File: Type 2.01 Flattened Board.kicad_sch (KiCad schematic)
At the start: 4 parts

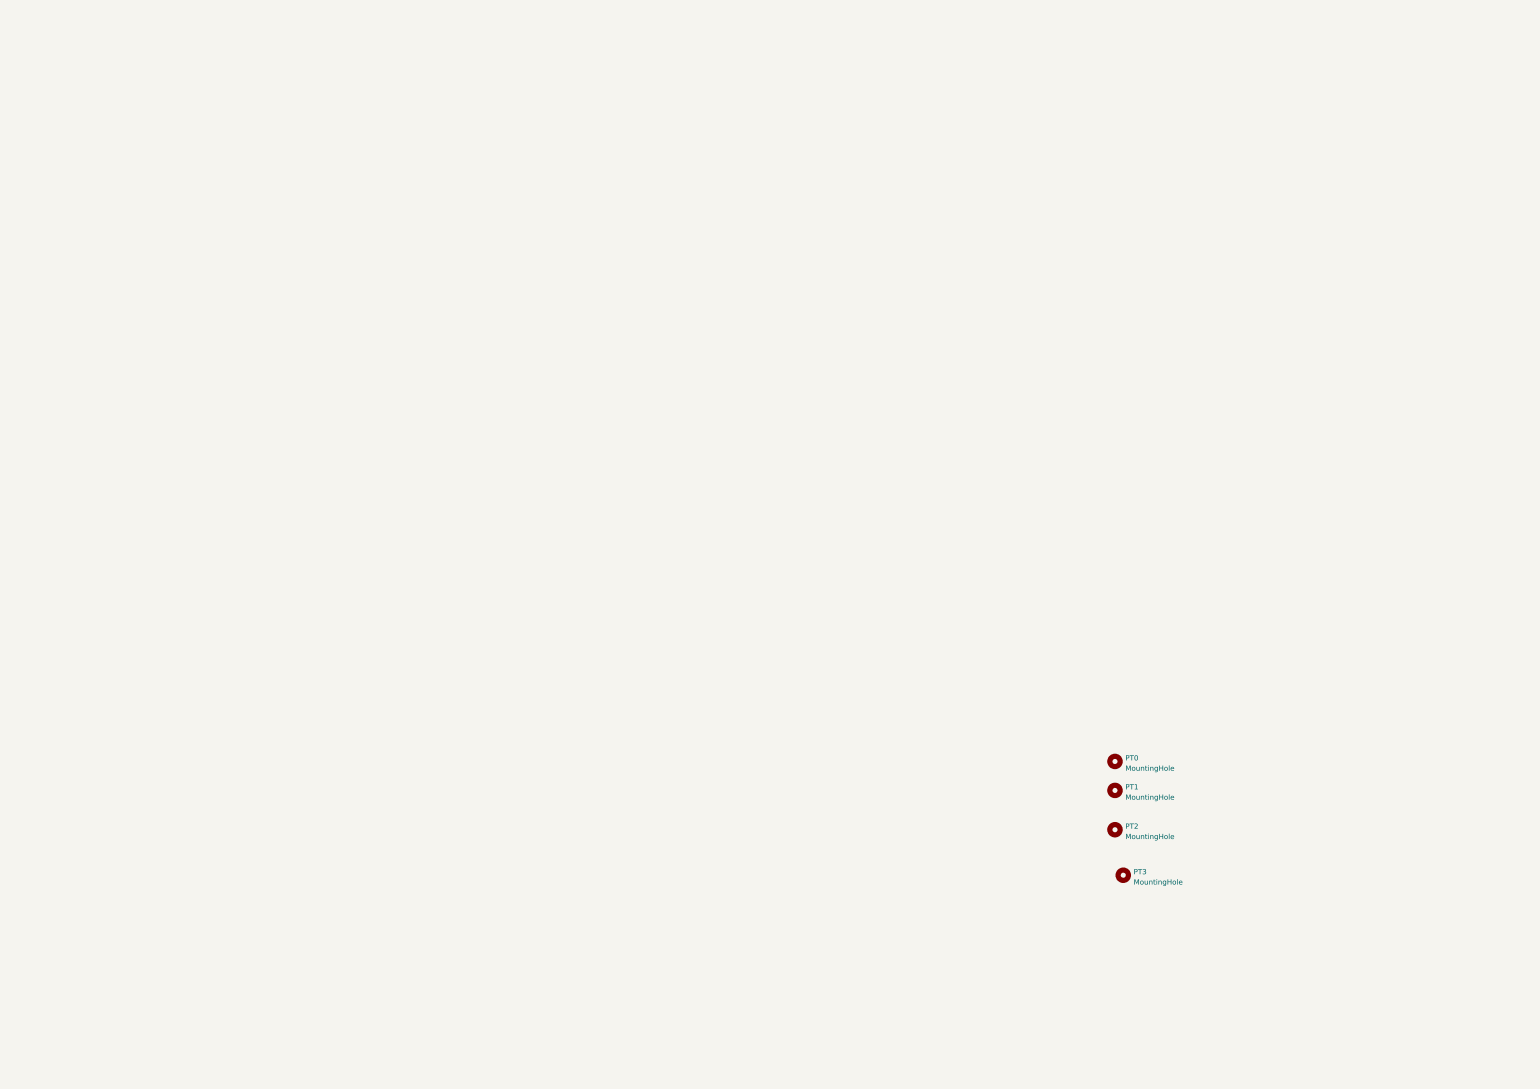
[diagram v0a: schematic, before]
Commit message: Start defining the pinout of the grand central m4
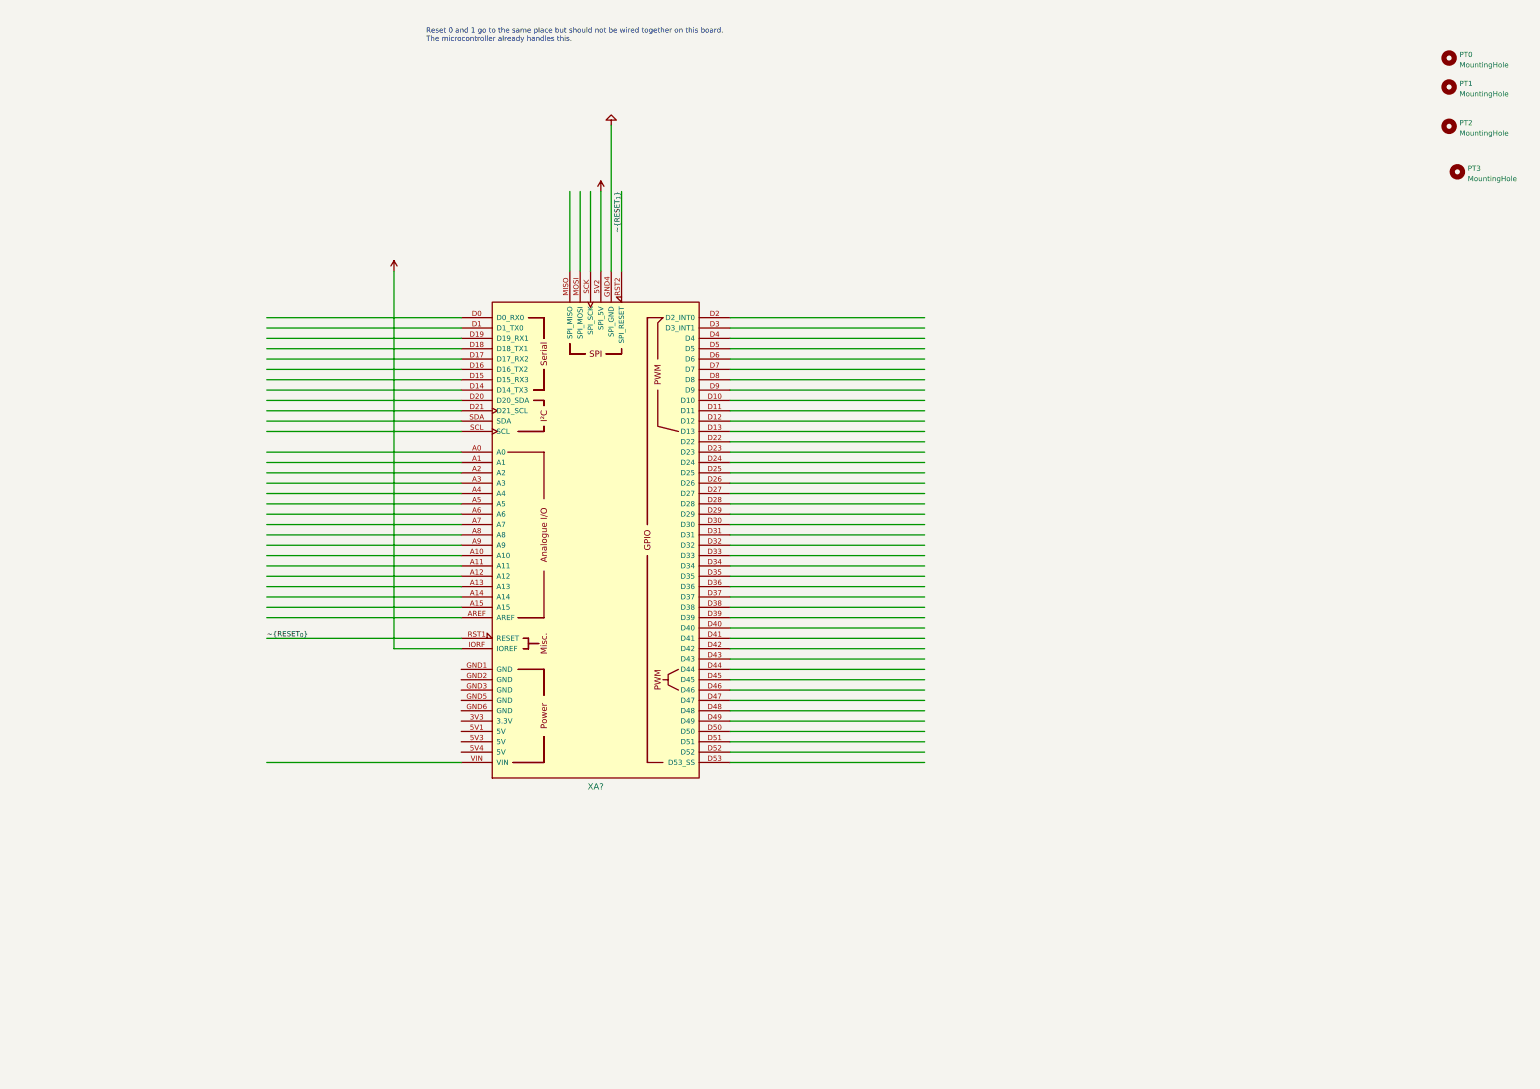
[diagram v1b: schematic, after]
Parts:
- added XA?: (no value), symbol arduino_alarm_siren:Arduino_Mega2560_Shield
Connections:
- new net +5V: XA?.5V2 (SPI_5V)
- new net GND: XA?.GND4 (SPI_GND)
- new net VCC: XA?.IORF (IOREF)
- new net ~{RESET_{0}}: XA?.RST1 (RESET)
- new net ~{RESET_{1}}: XA?.RST2 (SPI_RESET)
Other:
- note added: "Reset 0 and 1 go to the same place but should not be wired together on this board. The microcontroller already handles this."
- moved on the sheet: PT0, PT1, PT2, PT3

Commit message: More bus pin out action
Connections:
- net +5V: now also XA?.5V1 (5V), XA?.5V3 (5V), XA?.5V4 (5V)
- net GND: now also XA?.GND1 (GND), XA?.GND2 (GND), XA?.GND3 (GND), XA?.GND5 (GND), XA?.GND6 (GND)
- net +3V3: now reaches XA?.3V3 (3.3V)
- net Analog0: now reaches XA?.A0
- net Analog1: now reaches XA?.A1
- net Analog10: now reaches XA?.A10
- net Analog11: now reaches XA?.A11
- net Analog12: now reaches XA?.A12
- net Analog13: now reaches XA?.A13
- net Analog14: now reaches XA?.A14
- net Analog15: now reaches XA?.A15
- net Analog2: now reaches XA?.A2
- net Analog3: now reaches XA?.A3
- net Analog4: now reaches XA?.A4
- net Analog5: now reaches XA?.A5
- net Analog6: now reaches XA?.A6
- net Analog7: now reaches XA?.A7
- net Analog8: now reaches XA?.A8
- net Analog9: now reaches XA?.A9
- net AREF: now reaches XA?.AREF
- net BUS.PB25: now reaches XA?.D0 (D0_RX0)
- net BUS.PB24: now reaches XA?.D1 (D1_TX0)
- net BUS.PB22: now reaches XA?.D10
- net BUS.PB23: now reaches XA?.D11
- net D12: now reaches XA?.D12
- net D13: now reaches XA?.D13
- net D14: now reaches XA?.D14 (D14_TX3)
- net D15: now reaches XA?.D15 (D15_RX3)
- net D16: now reaches XA?.D16 (D16_TX2)
- net D17: now reaches XA?.D17 (D17_RX2)
- net D18: now reaches XA?.D18 (D18_TX1)
- net D19: now reaches XA?.D19 (D19_RX1)
- net BUS.PC18: now reaches XA?.D2 (D2_INT0)
- net BUS.PB20: now reaches XA?.D20 (D20_SDA)
- net BUS.PB21: now reaches XA?.D21 (D21_SCL)
- net BUS.PD12: now reaches XA?.D22
- net BUS.PA15: now reaches XA?.D23
- net BUS.PC17: now reaches XA?.D24
- net BUS.PC16: now reaches XA?.D25
- net D26: now reaches XA?.D26
- net D27: now reaches XA?.D27
- net D28: now reaches XA?.D28
- net D29: now reaches XA?.D29
- net BUS.PC19: now reaches XA?.D3 (D3_INT1)
- net D30: now reaches XA?.D30
- net D31: now reaches XA?.D31
- net D32: now reaches XA?.D32
- net D33: now reaches XA?.D33
- net D34: now reaches XA?.D34
- net D35: now reaches XA?.D35
- net D36: now reaches XA?.D36
- net D37: now reaches XA?.D37
- net D38: now reaches XA?.D38
- net D39: now reaches XA?.D39
- net BUS.PC20: now reaches XA?.D4
- net D40: now reaches XA?.D40
- net D41: now reaches XA?.D41
- net D42: now reaches XA?.D42
- net D43: now reaches XA?.D43
- net BUS.PC11: now reaches XA?.D44
- net BUS.PC10: now reaches XA?.D45
- net BUS.PC06: now reaches XA?.D46
- net BUS.PC07: now reaches XA?.D47
- net BUS.PC04: now reaches XA?.D48
- net BUS.PC05: now reaches XA?.D49
- net BUS.PC21: now reaches XA?.D5
- net MISO: now reaches XA?.D50
- net MOSI: now reaches XA?.D51
- net SCK: now reaches XA?.D52
- net ~{CS}: now reaches XA?.D53 (D53_SS)
- net BUS.PD20: now reaches XA?.D6
- net BUS.PD21: now reaches XA?.D7
- net BUS.PB18: now reaches XA?.D8
- net D9: now reaches XA?.D9
- net SPI_MISO: now reaches XA?.MISO (SPI_MISO)
- net SPI_MOSI: now reaches XA?.MOSI (SPI_MOSI)
- net SPI_SCK: now reaches XA?.SCK (SPI_SCK)
- net SCL_UNO: now reaches XA?.SCL
- net SDA_UNO: now reaches XA?.SDA
- net VIN: now reaches XA?.VIN
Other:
- note added: "Reset 0 and 1 go to the same place but should not be wired together on this board. The microcontroller already handles this. Same thing with SDA/SCL and the ICSP and miso connectors"
- note removed: "Reset 0 and 1 go to the same place but should not be wired together on this board. The microcontroller already handles this."

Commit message: Got the bus pinout done
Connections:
- net D12 renamed BUS.PB0
- net D13 renamed BUS.PB1
- net D14 renamed BUS.PB16
- net D15 renamed BUS.PB17
- net D16 renamed BUS.PC22
- net D17 renamed BUS.PC23
- net D18 renamed BUS.PB12
- net D19 renamed BUS.PB13
- net D26 renamed BUS.PA12
- net D27 renamed BUS.PA13
- net D28 renamed BUS.PA14
- net D29 renamed BUS.PB19
- net D30 renamed BUS.PA23
- net D31 renamed BUS.PA22
- net D32 renamed BUS.PA21
- net D33 renamed BUS.PA20
- net D34 renamed BUS.PA19
- net D35 renamed BUS.PA18
- net D36 renamed BUS.PA17
- net D37 renamed BUS.PA16
- net D38 renamed BUS.PB15
- net D39 renamed BUS.PB14
- net D40 renamed BUS.PC13
- net D41 renamed BUS.PC12
- net D42 renamed BUS.PC15
- net D43 renamed BUS.PC14
- net D9 renamed BUS.PB2

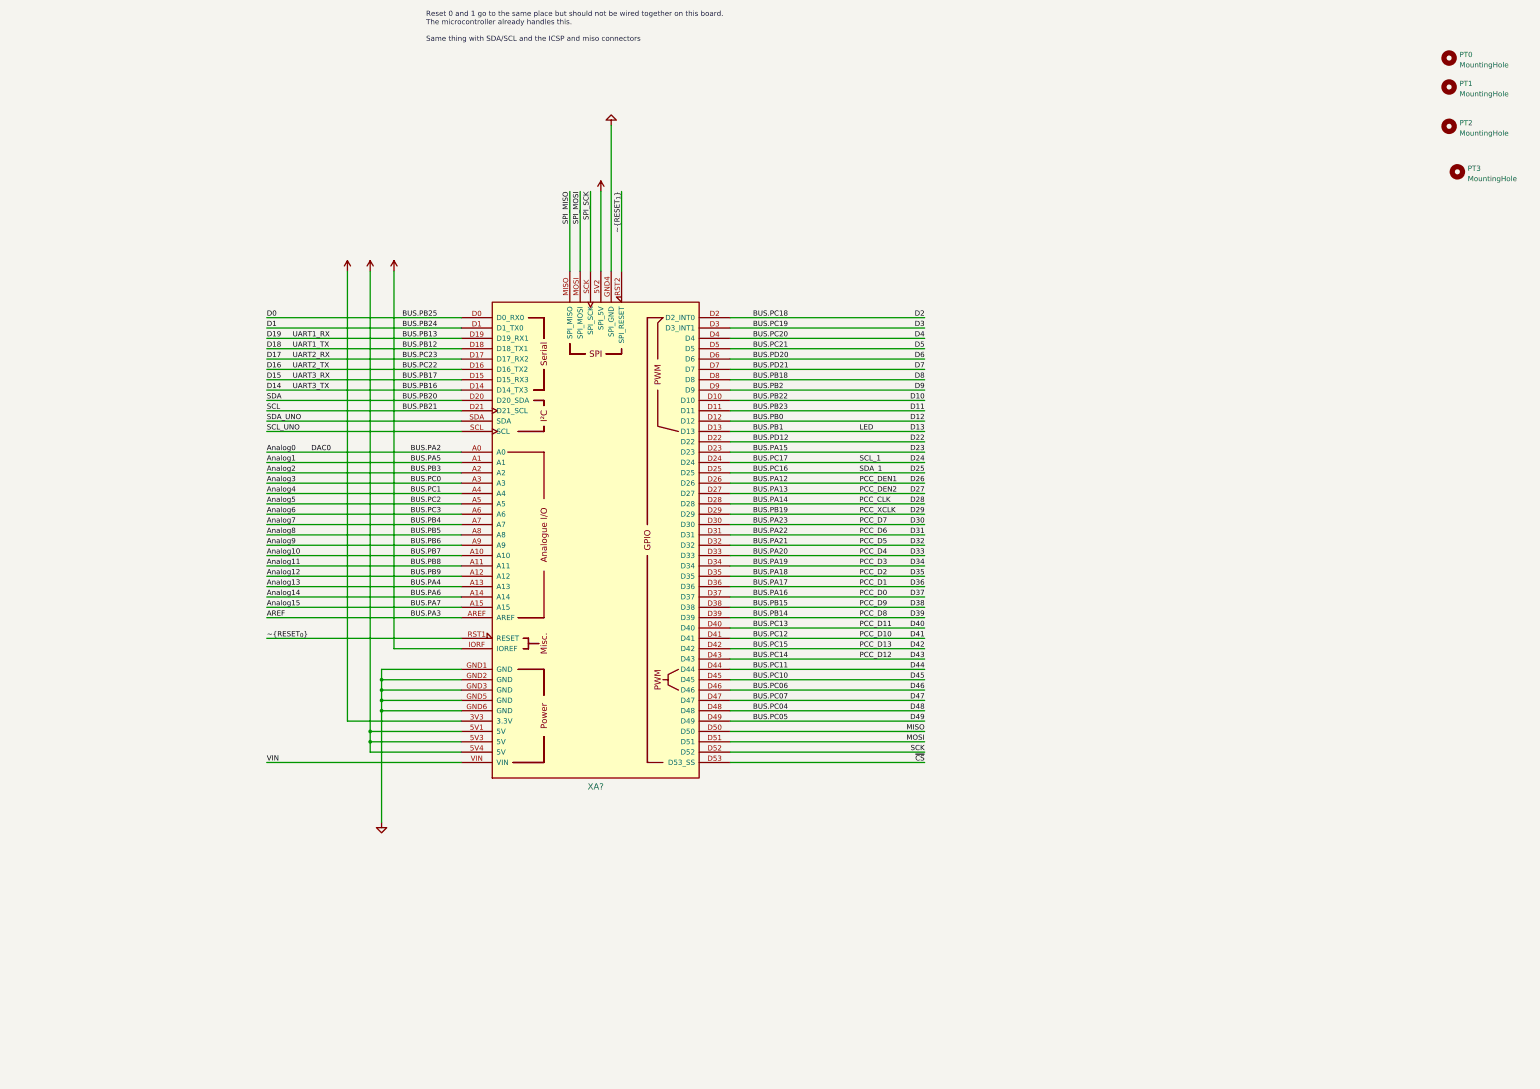
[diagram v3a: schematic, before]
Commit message: Added arduino uno shield port
Idea is to try and use the arduino uno pin numbers to make library usage
that much easier!
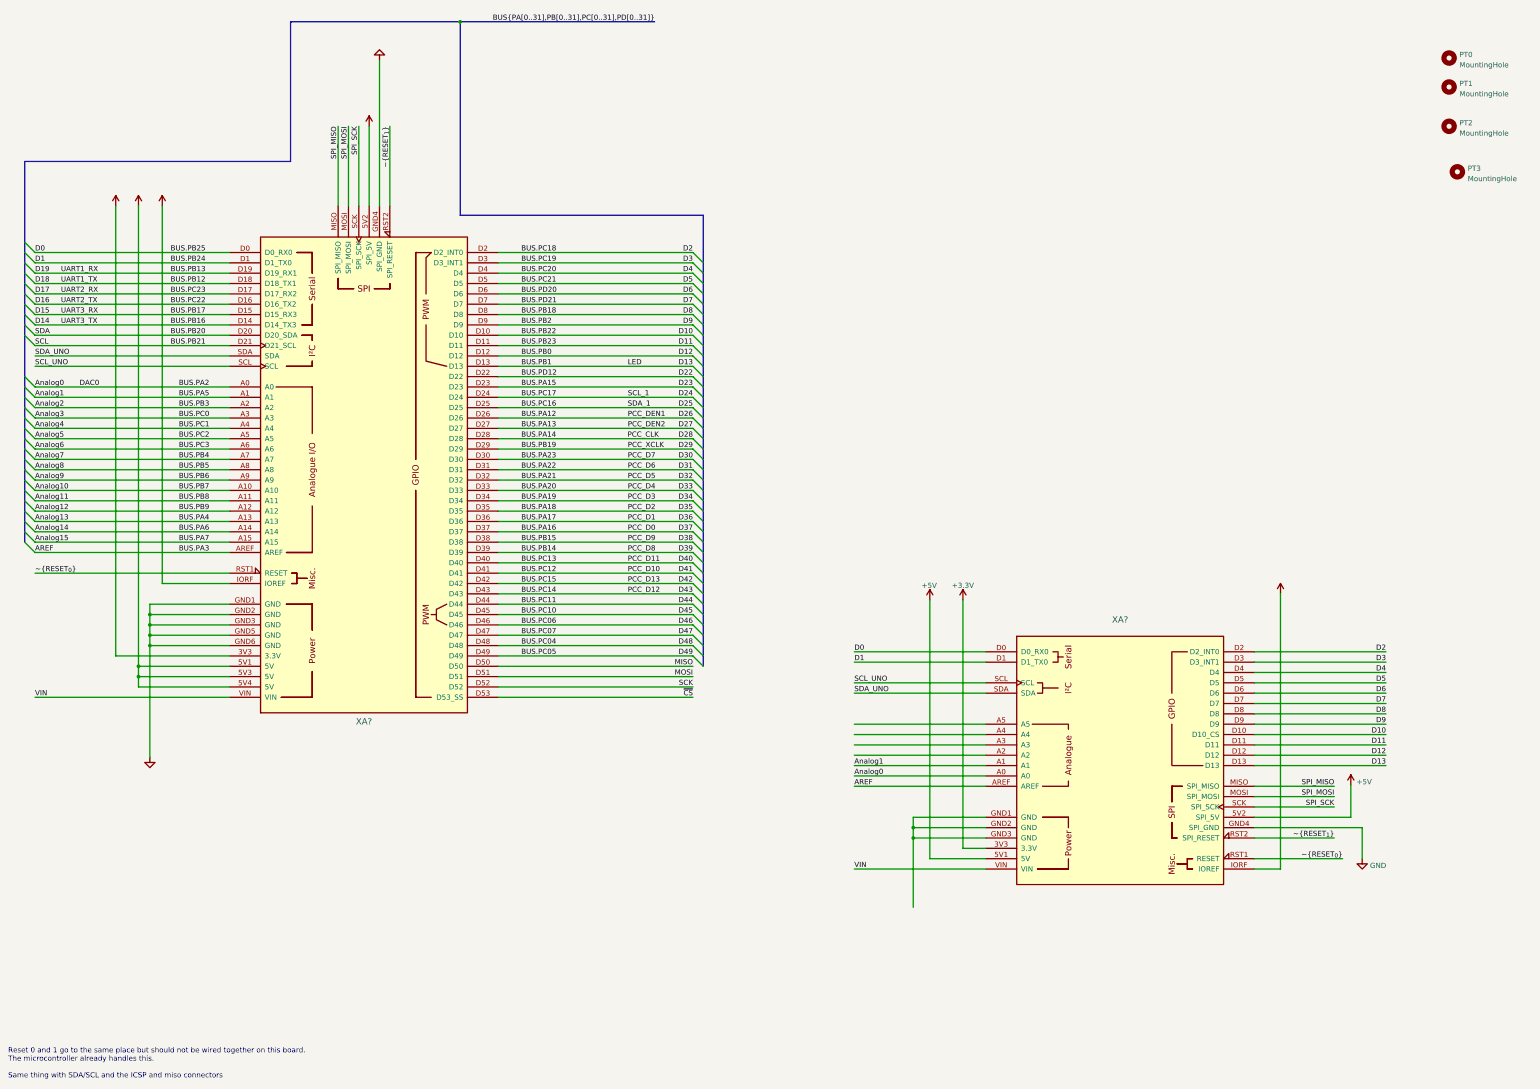
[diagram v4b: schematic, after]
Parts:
- added XA?: (no value), symbol arduino_alarm_siren:Arduino_Uno_Shield
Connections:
- net +3V3: now also XA?.3V3 (3.3V)
- net +5V: now also XA?.5V1 (5V), XA?.5V2 (SPI_5V)
- net AREF: now also XA?.AREF
- net Analog0: now also XA?.A0
- net Analog1: now also XA?.A1
- net BUS.PB0: now also XA?.D12
- net BUS.PB1: now also XA?.D13
- net BUS.PB18: now also XA?.D8
- net BUS.PB2: now also XA?.D9
- net BUS.PB22: now also XA?.D10 (D10_CS)
- net BUS.PB23: now also XA?.D11
- net BUS.PB24: now also XA?.D1 (D1_TX0)
- net BUS.PB25: now also XA?.D0 (D0_RX0)
- net BUS.PC18: now also XA?.D2 (D2_INT0)
- net BUS.PC19: now also XA?.D3 (D3_INT1)
- net BUS.PC20: now also XA?.D4
- net BUS.PC21: now also XA?.D5
- net BUS.PD20: now also XA?.D6
- net BUS.PD21: now also XA?.D7
- net GND: now also XA?.GND4 (SPI_GND)
- net SCL_UNO: now also XA?.SCL
- net SDA_UNO: now also XA?.SDA
- net SPI_MISO: now also XA?.MISO (SPI_MISO)
- net SPI_MOSI: now also XA?.MOSI (SPI_MOSI)
- net SPI_SCK: now also XA?.SCK (SPI_SCK)
- net VCC: now also XA?.IORF (IOREF)
- net VIN: now also XA?.VIN
- net ~{RESET_{0}}: now also XA?.RST1 (RESET)
- net ~{RESET_{1}}: now also XA?.RST2 (SPI_RESET)
- new net: XA?.GND1 (GND), XA?.GND2 (GND), XA?.GND3 (GND)
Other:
- moved on the sheet: XA?

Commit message: Fix up analog pinout so that reading and writing data lines is as efficient as possible
It does require using some of the analog pins that would be found in the
uno section. Just use some of the other analog pins found in the
extended set instead.
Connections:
- net Analog2: now also XA?.A2
- net Analog7: now also XA?.A3
- net Analog8: now also XA?.A4
- net Analog9: now also XA?.A5
- net BUS.PC04 renamed BUS.PC4
- net BUS.PC05 renamed BUS.PC5
- net BUS.PC06 renamed BUS.PC6
- net BUS.PC07 renamed BUS.PC7
